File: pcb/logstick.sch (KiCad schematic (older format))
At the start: 12 parts, among them IC1 ATTINY85-P, K1 USB, K2 DHT44, K3 SWITCH

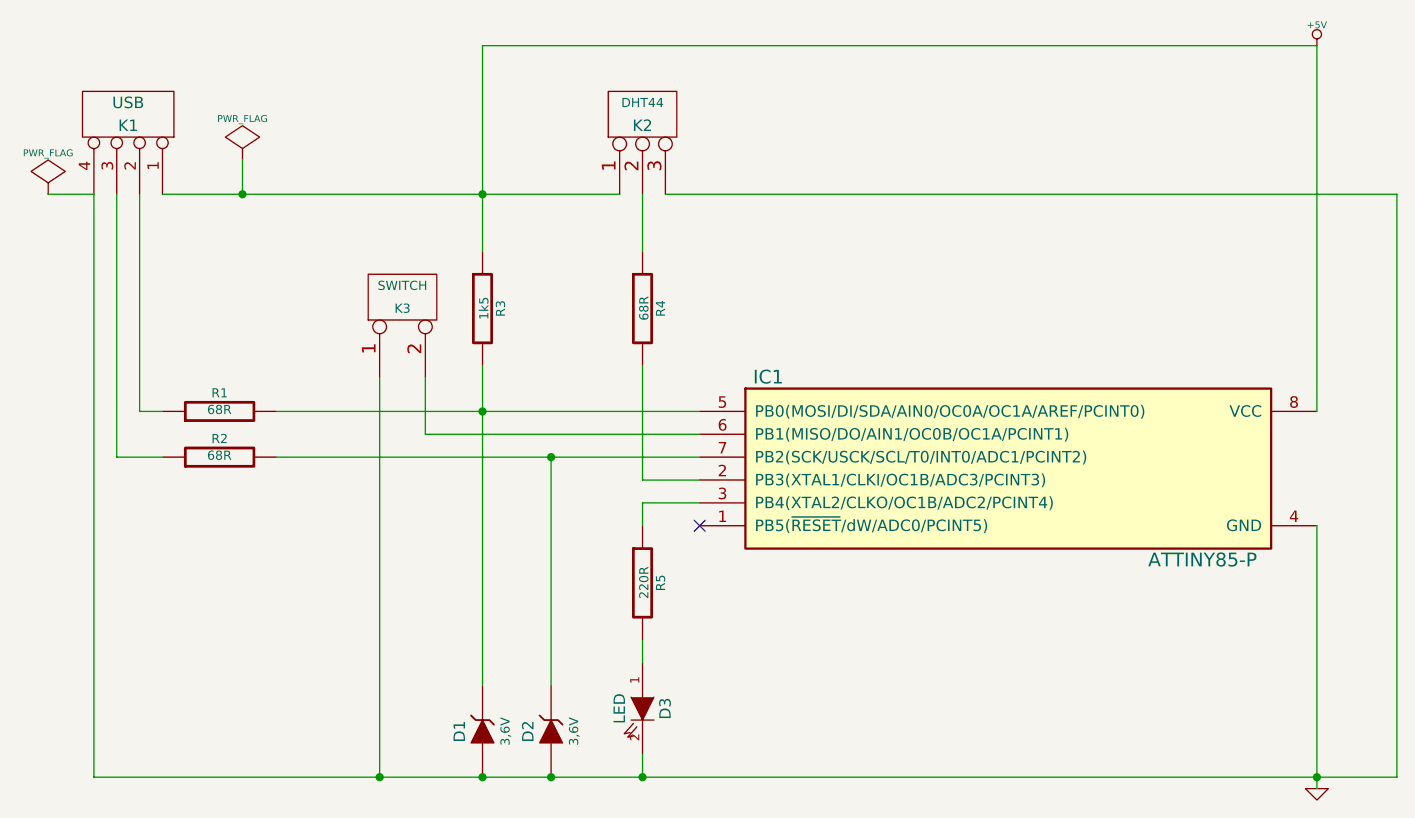
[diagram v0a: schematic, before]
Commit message: correction R68
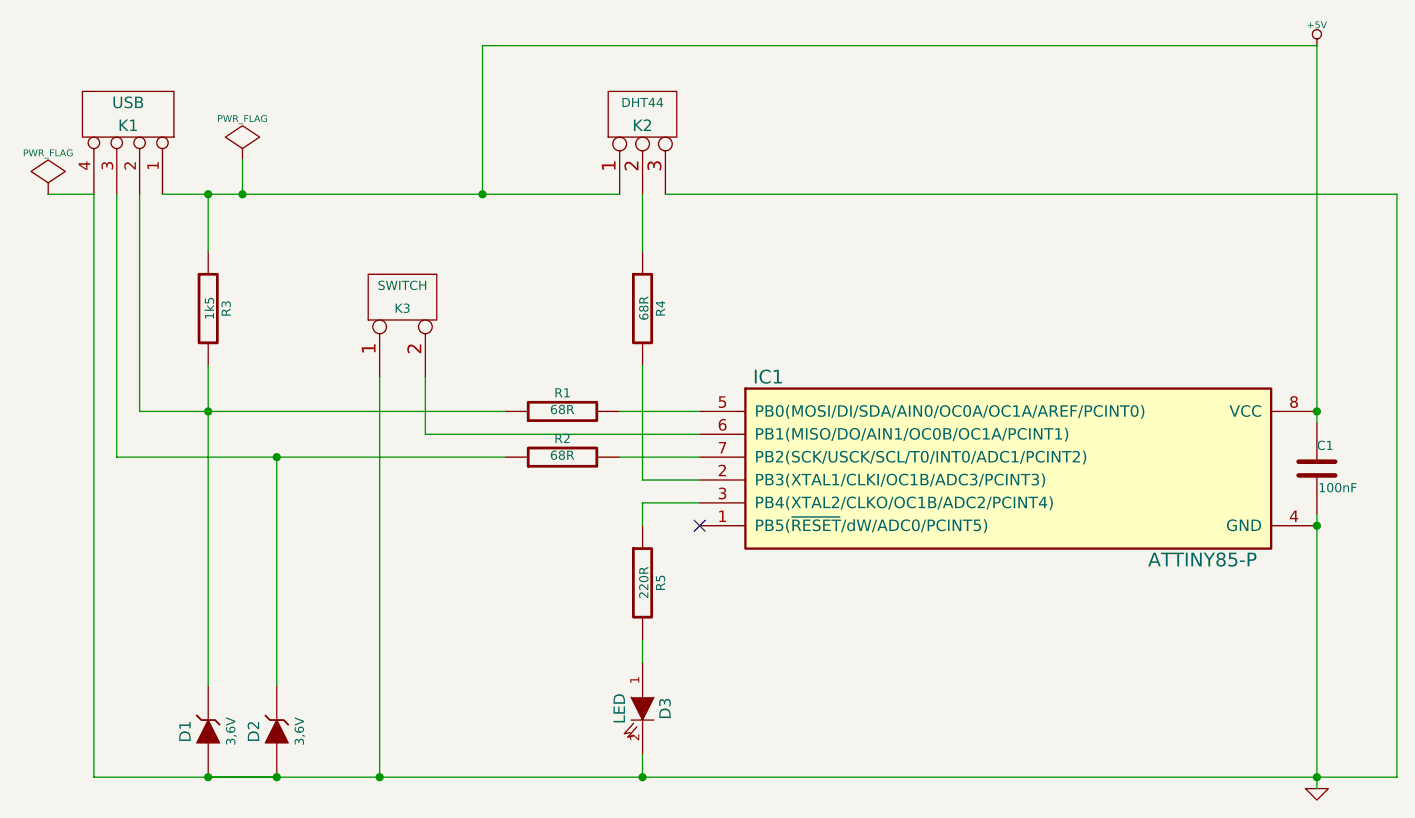
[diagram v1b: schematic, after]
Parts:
- added C1: 100nF, ~, symbol C
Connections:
- net +5V: now also C1.1
- net GND: now also C1.2
- net at IC1.5 (PB0(MOSI/DI/SDA/AIN0/OC0A/OC1A/AREF/PCINT0)), R1.2: no longer D1.2 (K), R3.2
- net at IC1.7 (PB2(SCK/USCK/SCL/T0/INT0/ADC1/PCINT2)), R2.2: no longer D2.2 (K)
- net at K1.2 (P2), R1.1: now also D1.2 (K), R3.2
- net at K1.3 (P3), R2.1: now also D2.2 (K)
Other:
- moved on the sheet: D1, D2, R1, R2, R3
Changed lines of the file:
@@
-EESchema Schematic File Version 2  date 21.05.2013 20:20:08
+EESchema Schematic File Version 2
 LIBS:power
 LIBS:device
@@
 Sheet 1 1
 Title ""
-Date "21 may 2013"
+Date "13 jun 2013"
 Rev ""
 Comp ""
@@
 $EndComp
 Wire Wire Line
-	7200 1450 7200 3050
+	7200 1450 7200 3100
 $Comp
 L R R1
 U 1 1 519BAD11
-P 2400 3050
-F 0 "R1" V 2480 3050 40  0000 C CNN
-F 1 "68R" V 2407 3051 40  0000 C CNN
-F 2 "~" V 2330 3050 30  0000 C CNN
-F 3 "~" H 2400 3050 30  0000 C CNN
-	1    2400 3050
+P 3900 3050
+F 0 "R1" V 3980 3050 40  0000 C CNN
+F 1 "68R" V 3907 3051 40  0000 C CNN
+F 2 "~" V 3830 3050 30  0000 C CNN
+F 3 "~" H 3900 3050 30  0000 C CNN
+	1    3900 3050
 	0    -1   -1   0
 $EndComp
@@
 L R R2
 U 1 1 519BAD67
-P 2400 3250
-F 0 "R2" V 2480 3250 40  0000 C CNN
-F 1 "68R" V 2407 3251 40  0000 C CNN
-F 2 "~" V 2330 3250 30  0000 C CNN
-F 3 "~" H 2400 3250 30  0000 C CNN
-	1    2400 3250
+P 3900 3250
+F 0 "R2" V 3980 3250 40  0000 C CNN
+F 1 "68R" V 3907 3251 40  0000 C CNN
+F 2 "~" V 3830 3250 30  0000 C CNN
+F 3 "~" H 3900 3250 30  0000 C CNN
+	1    3900 3250
 	0    -1   -1   0
 $EndComp
@@
 L R R3
 U 1 1 519BAD76
-P 3550 2600
-F 0 "R3" V 3630 2600 40  0000 C CNN
-F 1 "1k5" V 3557 2601 40  0000 C CNN
-F 2 "~" V 3480 2600 30  0000 C CNN
-F 3 "~" H 3550 2600 30  0000 C CNN
-	1    3550 2600
+P 2350 2600
+F 0 "R3" V 2430 2600 40  0000 C CNN
+F 1 "1k5" V 2357 2601 40  0000 C CNN
+F 2 "~" V 2280 2600 30  0000 C CNN
+F 3 "~" H 2350 2600 30  0000 C CNN
+	1    2350 2600
 	1    0    0    -1
 $EndComp
@@
 L ZENER D1
 U 1 1 519BAD9D
-P 3550 4450
-F 0 "D1" H 3550 4550 50  0000 C CNN
-F 1 "3,6V" H 3550 4350 40  0000 C CNN
-F 2 "~" H 3550 4450 60  0000 C CNN
-F 3 "~" H 3550 4450 60  0000 C CNN
-	1    3550 4450
+P 2350 4450
+F 0 "D1" H 2350 4550 50  0000 C CNN
+F 1 "3,6V" H 2350 4350 40  0000 C CNN
+F 2 "~" H 2350 4450 60  0000 C CNN
+F 3 "~" H 2350 4450 60  0000 C CNN
+	1    2350 4450
 	0    -1   -1   0
 $EndComp
@@
 L ZENER D2
 U 1 1 519BADAC
-P 3850 4450
-F 0 "D2" H 3850 4550 50  0000 C CNN
-F 1 "3,6V" H 3850 4350 40  0000 C CNN
-F 2 "~" H 3850 4450 60  0000 C CNN
-F 3 "~" H 3850 4450 60  0000 C CNN
-	1    3850 4450
+P 2650 4450
+F 0 "D2" H 2650 4550 50  0000 C CNN
+F 1 "3,6V" H 2650 4350 40  0000 C CNN
+F 2 "~" H 2650 4450 60  0000 C CNN
+F 3 "~" H 2650 4450 60  0000 C CNN
+	1    2650 4450
 	0    -1   -1   0
 $EndComp
@@
 $EndComp
 Wire Wire Line
-	2650 3050 4500 3050
-Wire Wire Line
-	3550 2850 3550 4250
-Connection ~ 3550 3050
-Wire Wire Line
-	2650 3250 4500 3250
-Wire Wire Line
-	2150 3050 2050 3050
+	4150 3050 4500 3050
+Wire Wire Line
+	2350 2850 2350 4250
+Connection ~ 2350 3050
+Wire Wire Line
+	4150 3250 4500 3250
+Wire Wire Line
+	2050 3050 3650 3050
 Wire Wire Line
 	2050 3050 2050 2100
 Wire Wire Line
-	2150 3250 1950 3250
+	1950 3250 3650 3250
 Wire Wire Line
 	1950 3250 1950 2100
@@
 	1850 4650 7550 4650
 Wire Wire Line
+	2650 4650 2350 4650
+Wire Wire Line
 	1850 4650 1850 2100
-Connection ~ 3550 4650
-Wire Wire Line
-	7200 3550 7200 4700
-Connection ~ 3850 4650
-Wire Wire Line
-	3850 3250 3850 4250
-Connection ~ 3850 3250
+Connection ~ 2350 4650
+Wire Wire Line
+	7200 3500 7200 4700
+Connection ~ 2650 4650
+Wire Wire Line
+	2650 3250 2650 4250
+Connection ~ 2650 3250
 $Comp
 L R R4
@@
 	4250 3350 4500 3350
 Wire Wire Line
-	3550 1450 3550 2350
+	3550 2100 3550 1450
+Wire Wire Line
+	2350 2100 2350 2350
 Wire Wire Line
 	2150 2100 4150 2100
 Connection ~ 3550 2100
 Wire Wire Line
-	7200 1450 3550 1450
+	3550 1450 7200 1450
 Wire Wire Line
 	7550 4650 7550 2100
@@
 	2500 1950 2500 2100
 Connection ~ 2500 2100
+Connection ~ 2350 2100
+$Comp
+L C C1
+U 1 1 51B9BB50
+P 7200 3300
+F 0 "C1" H 7200 3400 40  0000 L CNN
+F 1 "100nF" H 7206 3215 40  0000 L CNN
+F 2 "~" H 7238 3150 30  0000 C CNN
+F 3 "~" H 7200 3300 60  0000 C CNN
+	1    7200 3300
+	1    0    0    -1
+$EndComp
+Connection ~ 7200 3050
+Connection ~ 7200 3550
 $EndSCHEMATC
